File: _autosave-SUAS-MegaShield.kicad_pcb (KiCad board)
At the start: 2 copper layers, 1 part

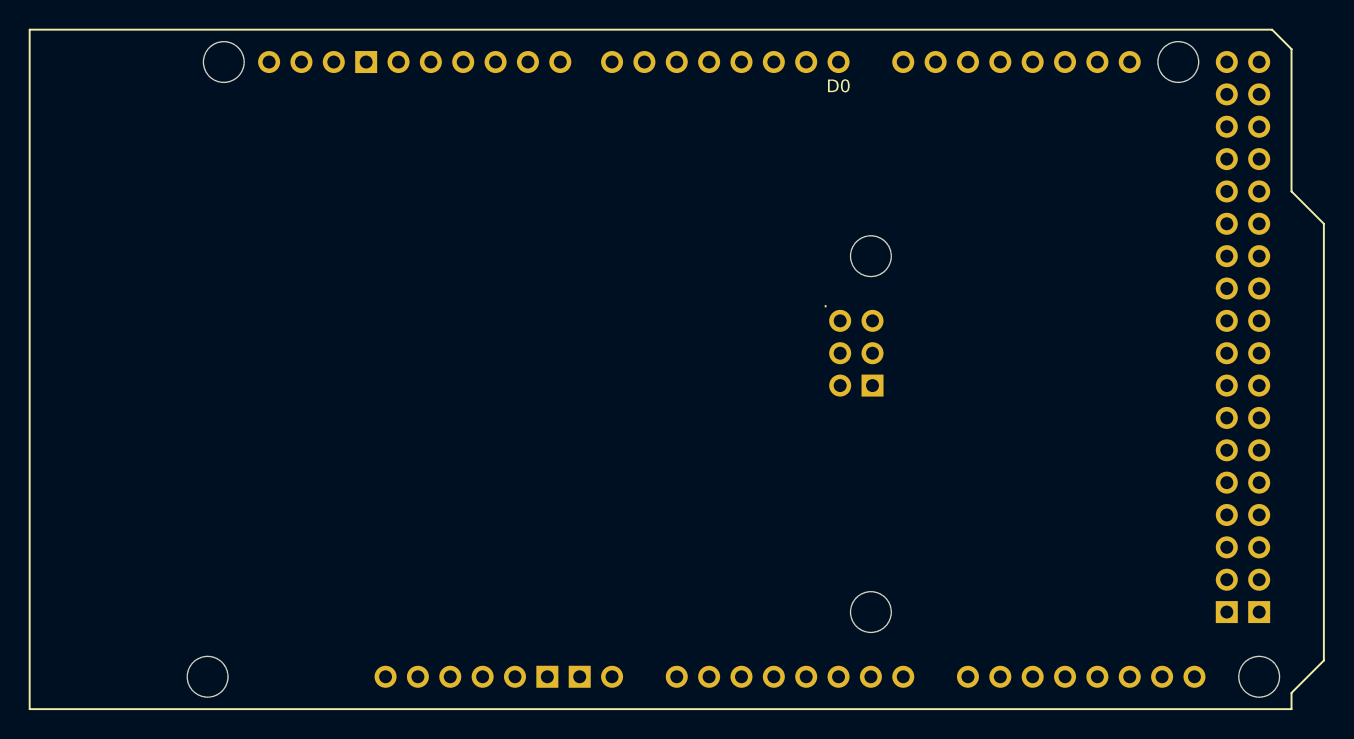
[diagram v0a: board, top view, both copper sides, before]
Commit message: Create arduino-kicad-library
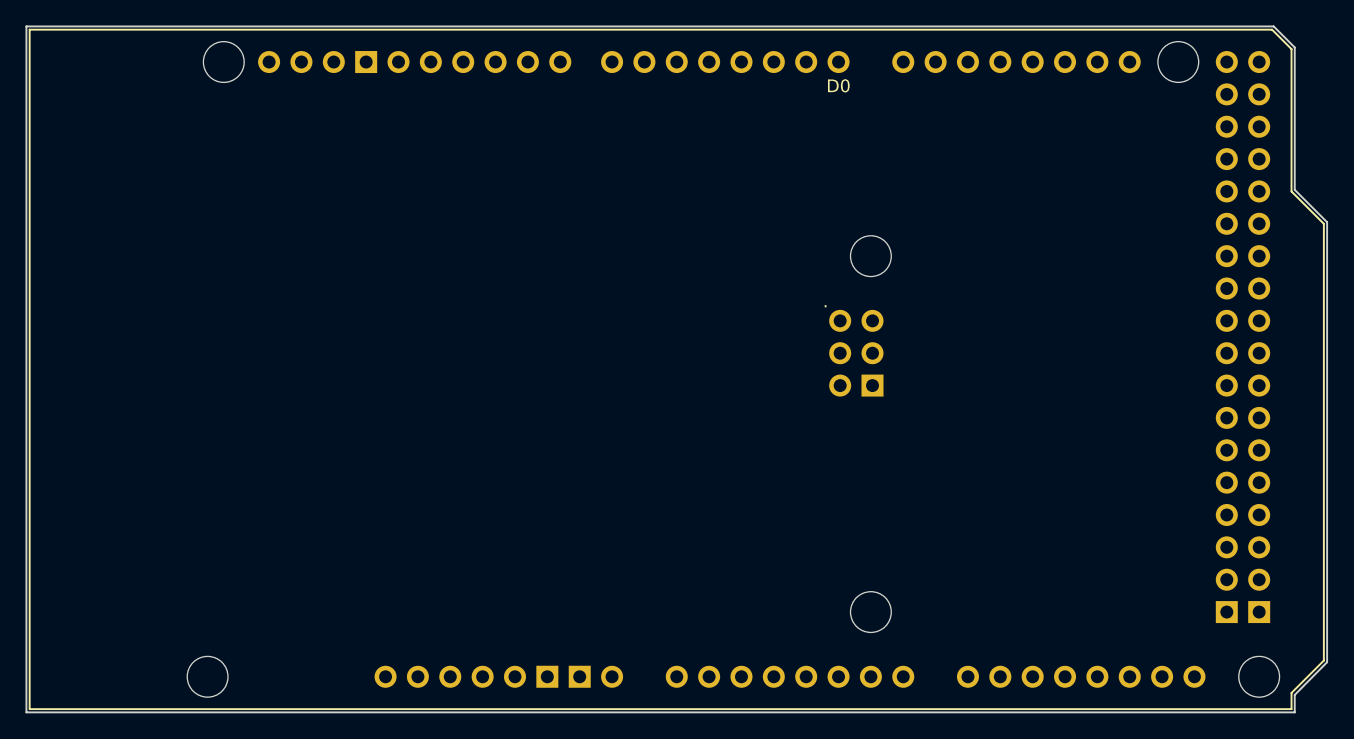
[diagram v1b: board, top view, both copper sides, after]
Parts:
- added ?: , clipboard:5463372f-7f41-4771-be05-13c3a7f8540b, F.Cu at (71.2, 82.4)
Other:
- board outline added: 102.1 x 53.8 mm
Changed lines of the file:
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@@
+		)
+	)
+	(footprint "clipboard:5463372f-7f41-4771-be05-13c3a7f8540b"
+		(layer "F.Cu")
+		(at 71.226 82.446)
+		(property "Reference" ""
+			(at 0 0 0)
+			(layer "F.SilkS")
+			(effects
+				(font
+					(size 1.27 1.27)
+					(thickness 0.15)
+				)
+			)
+		)
+		(property "Value" ""
+			(at 0 0 0)
+			(layer "F.Fab")
+			(effects
+				(font
+					(size 1.27 1.27)
+					(thickness 0.15)
+				)
+			)
+		)
+		(property "Footprint" ""
+			(at 0 0 0)
+			(layer "F.Fab")
+			(hide yes)
+			(effects
+				(font
+					(size 1.27 1.27)
+					(thickness 0.15)
+				)
+			)
+		)
+		(property "Datasheet" ""
+			(at 0 0 0)
+			(layer "F.Fab")
+			(hide yes)
+			(effects
+				(font
+					(size 1.27 1.27)
+					(thickness 0.15)
+				)
+			)
+		)
+		(property "Description" ""
+			(at 0 0 0)
+			(layer "F.Fab")
+			(hide yes)
+			(effects
+				(font
+					(size 1.27 1.27)
+					(thickness 0.15)
+				)
+			)
+		)
+		(fp_line
+			(start 0 53.848)
+			(end 0 0)
+			(stroke
+				(width 0.15)
+				(type solid)
+			)
+			(layer "Edge.Cuts")
+		)
+		(fp_line
+			(start 97.917 0)
+			(end 0 0)
+			(stroke
+				(width 0.15)
+				(type solid)
+			)
+			(layer "Edge.Cuts")
+		)
+		(fp_line
+			(start 99.564 52.484)
+			(end 99.568 53.848)
+			(stroke
+				(width 0.15)
+				(type solid)
+			)
+			(layer "Edge.Cuts")
+		)
+		(fp_line
+			(start 99.568 1.651)
+			(end 97.917 0)
+			(stroke
+				(width 0.15)
+				(type solid)
+			)
+			(layer "Edge.Cuts")
+		)
+		(fp_line
+			(start 99.568 1.651)
+			(end 99.568 12.827)
+			(stroke
+				(width 0.15)
+				(type solid)
+			)
+			(layer "Edge.Cuts")
+		)
+		(fp_line
+			(start 99.568 12.827)
+			(end 102.108 15.367)
+			(stroke
+				(width 0.15)
+				(type solid)
+			)
+			(layer "Edge.Cuts")
+		)
+		(fp_line
+			(start 99.568 53.848)
+			(end 0 53.848)
+			(stroke
+				(width 0.15)
+				(type solid)
+			)
+			(layer "Edge.Cuts")
+		)
+		(fp_line
+			(start 102.108 15.367)
+			(end 102.108 49.911)
+			(stroke
+				(width 0.15)
+				(type solid)
+			)
+			(layer "Edge.Cuts")
+		)
+		(fp_line
+			(start 102.108 49.911)
+			(end 99.564 52.484)
+			(stroke
+				(width 0.15)
+				(type solid)
+			)
+			(layer "Edge.Cuts")
 		)
 	)
